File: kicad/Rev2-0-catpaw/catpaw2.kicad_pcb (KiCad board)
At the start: 2 copper layers, 79 x 39 mm, 27 parts, among them J1 Conn_01x01_Socket_red, J2 Conn_01x01_Socket_black, J3 m12,Acode,5pin,femalesocket (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, U1 INA826, U2 LM1458mx

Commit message: routed rev2.0
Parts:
- added J4: Conn_01x03_Pin, Connector_PinHeader_2.54mm:PinHeader_1x03_P2.54mm_Vertical, F.Cu at (163.3, 92.2)
- D5: footprint LED_THT:LED_D5.0mm_Horizontal_O1.27mm_Z3.0mm -> LED_THT:LED_D3.0mm_Horizontal_O1.27mm_Z2.0mm; moved to B.Cu
- moved D5 3.51 mm to (180.0, 79.5), turned to -90 degrees
- moved R14 2.90 mm to (175.5, 79.5)
- moved R21 2.03 mm to (167.4, 96.2), turned to 90 degrees
- moved R13 1.47 mm to (165.1, 86.0), turned to 0 degrees
- moved C3 1.05 mm to (159.9, 79.9)
- moved C1 0.86 mm to (148.0, 91.7)
- moved R11 0.76 mm to (140.8, 95.6)
- moved C2 0.74 mm to (148.1, 99.4)
- moved R16 0.51 mm to (153.3, 85.1)
- moved R15 0.51 mm to (151.1, 82.9)
- moved R12 0.49 mm to (164.2, 82.8)
- moved R7 0.41 mm to (140.4, 103.6)
- moved R8 0.41 mm to (140.4, 87.9)
- moved R10 0.20 mm to (138.9, 91.3)
- moved R9 0.20 mm to (138.9, 100.1)
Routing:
- net /Vcc+: track 0.00 -> 50.5 mm, vias 0 -> 6
- net /Vcc-: track 0.00 -> 47.3 mm, vias 0 -> 5
- net Net-(D5-A): track 0.00 -> 31.2 mm
- net /In+ Analog Input: track 0.00 -> 24.3 mm
- net /VACin+: track 0.00 -> 11.7 mm
- net /VACin-: track 0.00 -> 11.6 mm
- net Net-(U1-+): track 0.00 -> 6.16 mm
- net Net-(U1--): track 0.00 -> 6.11 mm
- net Net-(U2A-+): track 0.00 -> 5.60 mm
- net Net-(U2B-+): track 0.00 -> 4.97 mm
- net Net-(R11-Pad2): track 0.00 -> 3.77 mm
- net Net-(R11-Pad1): track 0.00 -> 3.77 mm
- net Net-(D5-K): track 0.00 -> 2.94 mm
- net Net-(R4-Pad1): track 0.00 -> 2.93 mm
- net Net-(R1-Pad1): track 0.00 -> 2.93 mm
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- added copper zone on F.Cu, net /Vcc+
- added copper zone on F.Cu, net /Vcc-
- added copper zone on F.Cu, net Net-(R10-Pad1)
- added copper zone on F.Cu, net Net-(R3-Pad1)
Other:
- board text added: "GND"
- board text added: "VCC"
- board text added: "VEE"
- board text added: "dimensions: 39mm wide (match plucker) 79mm long (1mm less than hammond case) banana jacks setback:14mm, 16mm apart m12 setback: 4.5mm, centered"
- board text removed: "check pluckerv03 for placement"
- board text removed: "dimensions: 39mm wide (match plucker) 79mm long (1mm less than hammond case)"

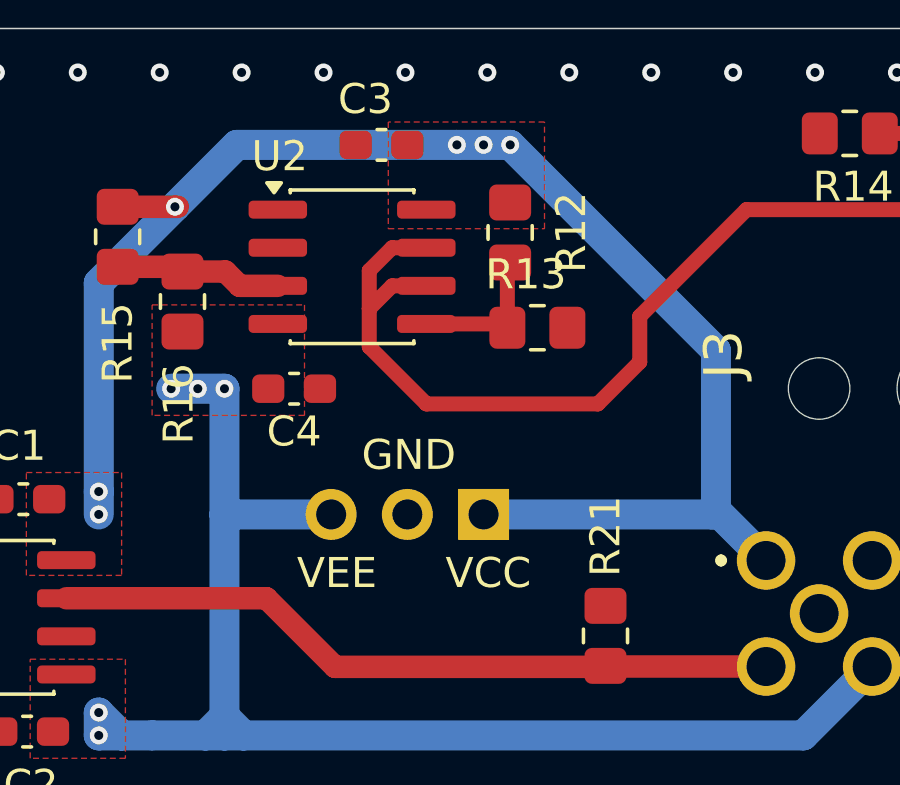
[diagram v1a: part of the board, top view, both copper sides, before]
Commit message: added fatpaw1.1 & catpaw2.0 gerbers
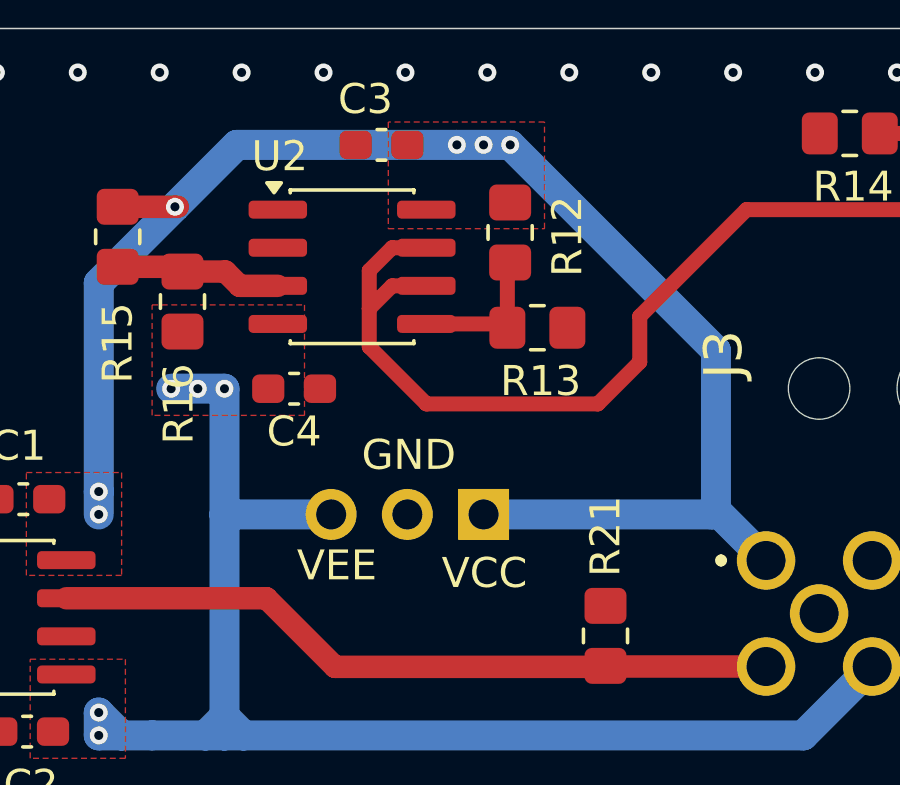
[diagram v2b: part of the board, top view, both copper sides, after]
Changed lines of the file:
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@@
 		(tags "resistor handsolder")
 		(property "Reference" "R13"
-			(at -0.381 -1.778 0)
+			(at 0.111 1.778 0)
 			(layer "F.SilkS")
 			(effects
@@
 		(tags "resistor handsolder")
 		(property "Reference" "R12"
-			(at 0 2.035 90)
+			(at -0.127 1.908 90)
 			(layer "F.SilkS")
 			(effects
@@
 	)
 	(gr_text "VCC"
-		(at 162.052 94.742 0)
+		(at 161.925 94.742 0)
 		(layer "F.SilkS")
 		(effects
@@
 	)
 	(gr_text "VEE"
-		(at 157.099 94.742 0)
+		(at 157.099 94.488 0)
 		(layer "F.SilkS")
 		(effects

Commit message: built catpaw rev2.0
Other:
- board text added: "led in way of the machine thread holes in case"
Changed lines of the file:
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@@
+		)
+	)
+	(gr_text "led in way of the machine thread holes in case"
+		(at 187.96 71.247 0)
+		(layer "User.2")
+		(effects
+			(font
+				(size 1 1)
+				(thickness 0.15)
+			)
+			(justify left bottom)
 		)
 	)
@@
 		(polygon
 			(pts
-				(xy 139.954 71.755) (xy 188.214 73.152) (xy 189.738 121.92) (xy 140.081 121.92)
+				(xy 139.954 73.152) (xy 187.325 73.152) (xy 187.325 116.078) (xy 139.7 116.586)
 			)
 		)
